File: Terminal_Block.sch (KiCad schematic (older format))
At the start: 0 parts

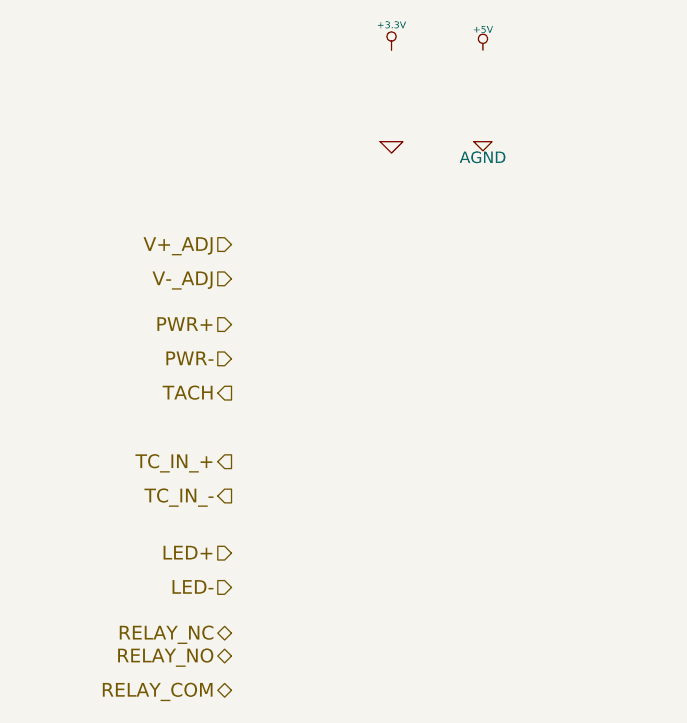
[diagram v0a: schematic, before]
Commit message: Terminal Blocks and ATX Connector
Created footprints for 12pin, 3pin terminal blocks and 24pin ATX Header.
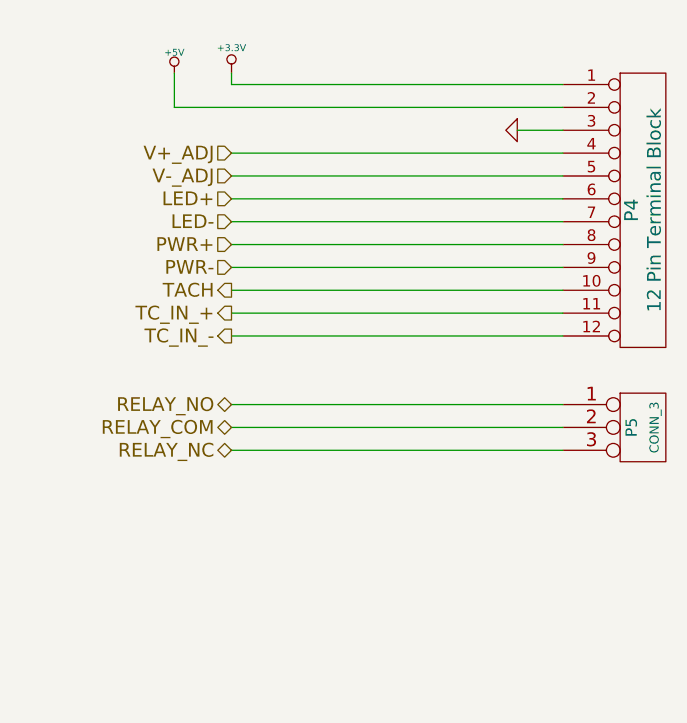
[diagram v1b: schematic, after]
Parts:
- added P4: 12 Pin Terminal Block, symbol CONN_12
- added P5: CONN_3, symbol CONN_3
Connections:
- net +3.3V: now also P4.1 (P1)
- net +5V: now also P4.2 (P2)
- net GND: now also P4.3 (P3)
- net LED+: now also P4.6 (P6)
- net LED-: now also P4.7 (P7)
- net PWR+: now also P4.8 (P8)
- net PWR-: now also P4.9 (P9)
- net RELAY_COM: now also P5.2 (PM)
- net RELAY_NC: now also P5.3 (P3)
- net RELAY_NO: now also P5.1 (P1)
- net TACH: now also P4.10 (P10)
- net TC_IN_+: now also P4.11 (P11)
- net TC_IN_-: now also P4.12 (P12)
- net V+_ADJ: now also P4.4 (P4)
- net V-_ADJ: now also P4.5 (P5)
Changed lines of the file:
@@
 Comment4 ""
 $EndDescr
+Text HLabel 4750 1100 0    60   Input ~ 0
+V+_ADJ
+Text HLabel 4750 1200 0    60   Input ~ 0
+V-_ADJ
 Text HLabel 4750 1500 0    60   Input ~ 0
-V+_ADJ
-Text HLabel 4750 1650 0    60   Input ~ 0
-V-_ADJ
-Text HLabel 4750 1850 0    60   Input ~ 0
 PWR+
-Text HLabel 4750 2000 0    60   Input ~ 0
+Text HLabel 4750 1600 0    60   Input ~ 0
 PWR-
-Text HLabel 4750 2150 0    60   Output ~ 0
+Text HLabel 4750 1700 0    60   Output ~ 0
 TACH
-Text HLabel 4750 2450 0    60   Output ~ 0
-TC_IN_+
-Text HLabel 4750 2600 0    60   Output ~ 0
-TC_IN_-
-Text HLabel 4750 2850 0    60   Input ~ 0
+Text HLabel 4750 1300 0    60   Input ~ 0
 LED+
-Text HLabel 4750 3000 0    60   Input ~ 0
+Text HLabel 4750 1400 0    60   Input ~ 0
 LED-
-Text HLabel 4750 3200 0    60   BiDi ~ 0
+Text HLabel 4750 2400 0    60   BiDi ~ 0
 RELAY_NC
-Text HLabel 4750 3300 0    60   BiDi ~ 0
+Text HLabel 4750 2200 0    60   BiDi ~ 0
 RELAY_NO
-Text HLabel 4750 3450 0    60   BiDi ~ 0
+Text HLabel 4750 2300 0    60   BiDi ~ 0
 RELAY_COM
 $Comp
 L +3.3V #PWR064
 U 1 1 52F91565
-P 5450 650
-F 0 "#PWR064" H 5450 610 30  0001 C CNN
-F 1 "+3.3V" H 5450 760 30  0000 C CNN
-F 2 "" H 5450 650 60  0000 C CNN
-F 3 "" H 5450 650 60  0000 C CNN
-	1    5450 650
+P 4750 750
+F 0 "#PWR064" H 4750 710 30  0001 C CNN
+F 1 "+3.3V" H 4750 860 30  0000 C CNN
+F 2 "" H 4750 750 60  0000 C CNN
+F 3 "" H 4750 750 60  0000 C CNN
+	1    4750 750
 	1    0    0    -1
 $EndComp
@@
 L +5V #PWR065
 U 1 1 52F91574
-P 5850 650
-F 0 "#PWR065" H 5850 740 20  0001 C CNN
-F 1 "+5V" H 5850 740 30  0000 C CNN
-F 2 "" H 5850 650 60  0000 C CNN
-F 3 "" H 5850 650 60  0000 C CNN
-	1    5850 650
+P 4500 750
+F 0 "#PWR065" H 4500 840 20  0001 C CNN
+F 1 "+5V" H 4500 840 30  0000 C CNN
+F 2 "" H 4500 750 60  0000 C CNN
+F 3 "" H 4500 750 60  0000 C CNN
+	1    4500 750
 	1    0    0    -1
 $EndComp
@@
 L GND #PWR066
 U 1 1 52F91583
-P 5450 1050
-F 0 "#PWR066" H 5450 1050 30  0001 C CNN
-F 1 "GND" H 5450 980 30  0001 C CNN
-F 2 "" H 5450 1050 60  0000 C CNN
-F 3 "" H 5450 1050 60  0000 C CNN
-	1    5450 1050
+P 6000 1000
+F 0 "#PWR066" H 6000 1000 30  0001 C CNN
+F 1 "GND" H 6000 930 30  0001 C CNN
+F 2 "" H 6000 1000 60  0000 C CNN
+F 3 "" H 6000 1000 60  0000 C CNN
+	1    6000 1000
+	0    1    1    0
+$EndComp
+$Comp
+L CONN_12 P4
+U 1 1 5309CB10
+P 6550 1350
+F 0 "P4" V 6500 1350 60  0000 C CNN
+F 1 "12 Pin Terminal Block" V 6600 1350 60  0000 C CNN
+F 2 "" H 6550 1350 60  0000 C CNN
+F 3 "" H 6550 1350 60  0000 C CNN
+F 4 "On-Shore Technology" H 6550 1350 60  0001 C CNN "MFG NAME"
+F 5 "OSTTE120104" H 6550 1350 60  0001 C CNN "MFG PART NUM"
+	1    6550 1350
 	1    0    0    -1
 $EndComp
+Wire Wire Line
+	4750 1200 6200 1200
+Wire Wire Line
+	6200 1100 4750 1100
+Wire Wire Line
+	6200 1000 6000 1000
+Wire Wire Line
+	4500 900  6200 900
+Wire Wire Line
+	4500 750  4500 900
+Wire Wire Line
+	4750 800  4750 750
+Wire Wire Line
+	6200 800  4750 800
+Wire Wire Line
+	4750 1300 6200 1300
+Wire Wire Line
+	4750 1400 6200 1400
+Wire Wire Line
+	4750 1500 6200 1500
+Wire Wire Line
+	4750 1600 6200 1600
+Text HLabel 4750 1900 0    60   Output ~ 0
+TC_IN_-
+Text HLabel 4750 1800 0    60   Output ~ 0
+TC_IN_+
+Wire Wire Line
+	4750 1700 6200 1700
+Wire Wire Line
+	4750 1800 6200 1800
+Wire Wire Line
+	4750 1900 6200 1900
 $Comp
-L AGND #PWR067
-U 1 1 52F91592
-P 5850 1050
-F 0 "#PWR067" H 5850 1050 40  0001 C CNN
-F 1 "AGND" H 5850 980 50  0000 C CNN
-F 2 "" H 5850 1050 60  0000 C CNN
-F 3 "" H 5850 1050 60  0000 C CNN
-	1    5850 1050
+L CONN_3 P5
+U 1 1 5309D123
+P 6550 2300
+F 0 "P5" V 6500 2300 50  0000 C CNN
+F 1 "CONN_3" V 6600 2300 40  0000 C CNN
+F 2 "" H 6550 2300 60  0000 C CNN
+F 3 "" H 6550 2300 60  0000 C CNN
+F 4 "PHOENIX CONTACT" H 6550 2300 60  0001 C CNN "MFG NAME"
+F 5 "1935174" H 6550 2300 60  0001 C CNN "MFG PART NUM"
+	1    6550 2300
 	1    0    0    -1
 $EndComp
+Wire Wire Line
+	4750 2200 6200 2200
+Wire Wire Line
+	4750 2300 6200 2300
+Wire Wire Line
+	4750 2400 6200 2400
 $EndSCHEMATC

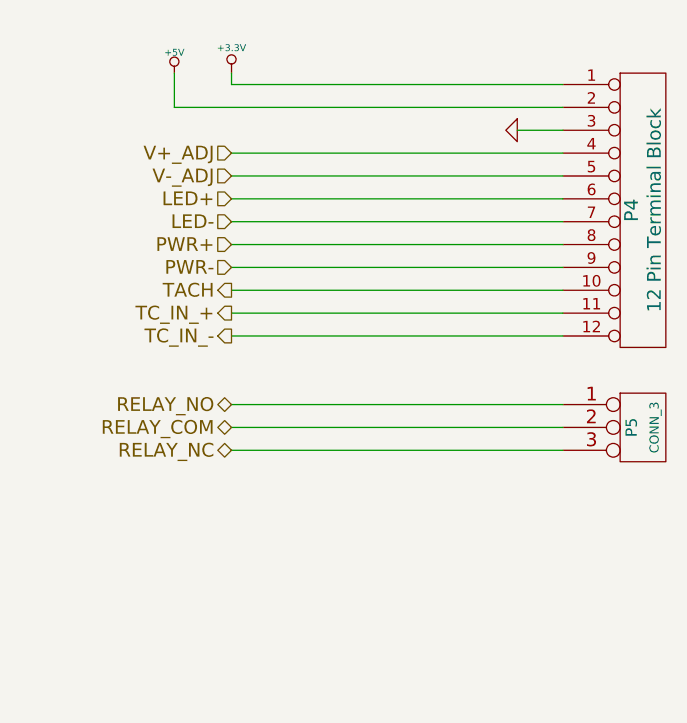
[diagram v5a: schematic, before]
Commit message: Layout v4.0
Adding ground planes according to location of modules
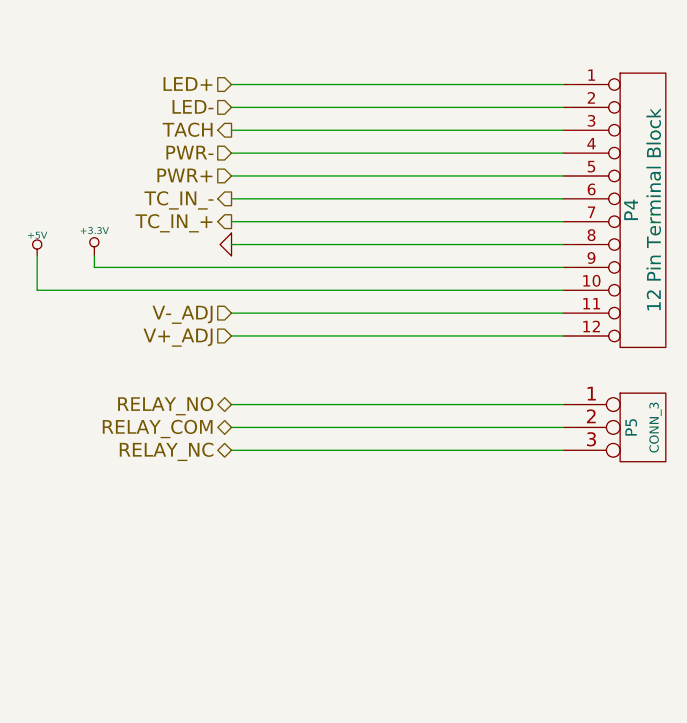
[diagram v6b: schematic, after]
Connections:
- net +3.3V: now also P4.9 (P9); no longer P4.1 (P1)
- net +5V: now also P4.10 (P10); no longer P4.2 (P2)
- net GND: now also P4.8 (P8); no longer P4.3 (P3)
- net LED+: now also P4.1 (P1); no longer P4.6 (P6)
- net LED-: now also P4.2 (P2); no longer P4.7 (P7)
- net PWR+: now also P4.5 (P5); no longer P4.8 (P8)
- net PWR-: now also P4.4 (P4); no longer P4.9 (P9)
- net TACH: now also P4.3 (P3); no longer P4.10 (P10)
- net TC_IN_+: now also P4.7 (P7); no longer P4.11 (P11)
- net TC_IN_-: now also P4.6 (P6); no longer P4.12 (P12)
- net V+_ADJ: now also P4.12 (P12); no longer P4.4 (P4)
- net V-_ADJ: now also P4.11 (P11); no longer P4.5 (P5)
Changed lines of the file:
@@
 Sheet 9 9
 Title ""
-Date "3 mar 2014"
+Date "6 mar 2014"
 Rev ""
 Comp ""
@@
 Comment4 ""
 $EndDescr
+Text HLabel 4750 1900 0    60   Input ~ 0
+V+_ADJ
+Text HLabel 4750 1800 0    60   Input ~ 0
+V-_ADJ
+Text HLabel 4750 1200 0    60   Input ~ 0
+PWR+
 Text HLabel 4750 1100 0    60   Input ~ 0
-V+_ADJ
-Text HLabel 4750 1200 0    60   Input ~ 0
-V-_ADJ
-Text HLabel 4750 1500 0    60   Input ~ 0
-PWR+
-Text HLabel 4750 1600 0    60   Input ~ 0
 PWR-
-Text HLabel 4750 1700 0    60   Output ~ 0
+Text HLabel 4750 1000 0    60   Output ~ 0
 TACH
-Text HLabel 4750 1300 0    60   Input ~ 0
+Text HLabel 4750 800  0    60   Input ~ 0
 LED+
-Text HLabel 4750 1400 0    60   Input ~ 0
+Text HLabel 4750 900  0    60   Input ~ 0
 LED-
 Text HLabel 4750 2400 0    60   BiDi ~ 0
@@
 RELAY_COM
 $Comp
-L +3.3V #PWR062
+L +3.3V #PWR060
 U 1 1 52F91565
-P 4750 750
-F 0 "#PWR062" H 4750 710 30  0001 C CNN
-F 1 "+3.3V" H 4750 860 30  0000 C CNN
-F 2 "" H 4750 750 60  0000 C CNN
-F 3 "" H 4750 750 60  0000 C CNN
-	1    4750 750
+P 4150 1550
+F 0 "#PWR060" H 4150 1510 30  0001 C CNN
+F 1 "+3.3V" H 4150 1660 30  0000 C CNN
+F 2 "" H 4150 1550 60  0000 C CNN
+F 3 "" H 4150 1550 60  0000 C CNN
+	1    4150 1550
 	1    0    0    -1
 $EndComp
 $Comp
-L +5V #PWR063
+L +5V #PWR061
 U 1 1 52F91574
-P 4500 750
-F 0 "#PWR063" H 4500 840 20  0001 C CNN
-F 1 "+5V" H 4500 840 30  0000 C CNN
-F 2 "" H 4500 750 60  0000 C CNN
-F 3 "" H 4500 750 60  0000 C CNN
-	1    4500 750
+P 3900 1550
+F 0 "#PWR061" H 3900 1640 20  0001 C CNN
+F 1 "+5V" H 3900 1640 30  0000 C CNN
+F 2 "" H 3900 1550 60  0000 C CNN
+F 3 "" H 3900 1550 60  0000 C CNN
+	1    3900 1550
 	1    0    0    -1
 $EndComp
 $Comp
-L GND #PWR064
+L GND #PWR062
 U 1 1 52F91583
-P 6000 1000
-F 0 "#PWR064" H 6000 1000 30  0001 C CNN
-F 1 "GND" H 6000 930 30  0001 C CNN
-F 2 "" H 6000 1000 60  0000 C CNN
-F 3 "" H 6000 1000 60  0000 C CNN
-	1    6000 1000
+P 4750 1500
+F 0 "#PWR062" H 4750 1500 30  0001 C CNN
+F 1 "GND" H 4750 1430 30  0001 C CNN
+F 2 "" H 4750 1500 60  0000 C CNN
+F 3 "" H 4750 1500 60  0000 C CNN
+	1    4750 1500
 	0    1    1    0
 $EndComp
@@
 $EndComp
 Wire Wire Line
-	4750 1200 6200 1200
+	3900 1550 3900 1700
 Wire Wire Line
-	6200 1100 4750 1100
-Wire Wire Line
-	6200 1000 6000 1000
-Wire Wire Line
-	4500 900  6200 900
-Wire Wire Line
-	4500 750  4500 900
-Wire Wire Line
-	4750 800  4750 750
-Wire Wire Line
-	6200 800  4750 800
-Wire Wire Line
-	4750 1300 6200 1300
-Wire Wire Line
-	4750 1400 6200 1400
-Wire Wire Line
-	4750 1500 6200 1500
-Wire Wire Line
-	4750 1600 6200 1600
-Text HLabel 4750 1900 0    60   Output ~ 0
+	4150 1600 4150 1550
+Text HLabel 4750 1300 0    60   Output ~ 0
 TC_IN_-
-Text HLabel 4750 1800 0    60   Output ~ 0
+Text HLabel 4750 1400 0    60   Output ~ 0
 TC_IN_+
-Wire Wire Line
-	4750 1700 6200 1700
-Wire Wire Line
-	4750 1800 6200 1800
-Wire Wire Line
-	4750 1900 6200 1900
 $Comp
 L CONN_3 P5
@@
 Wire Wire Line
 	4750 2400 6200 2400
+Wire Wire Line
+	4150 1600 6200 1600
+Wire Wire Line
+	3900 1700 6200 1700
+Wire Wire Line
+	4750 800  6200 800
+Wire Wire Line
+	6200 900  4750 900
+Wire Wire Line
+	4750 1800 6200 1800
+Wire Wire Line
+	4750 1900 6200 1900
+Wire Wire Line
+	4750 1200 6200 1200
+Wire Wire Line
+	6200 1100 4750 1100
+Wire Wire Line
+	4750 1000 6200 1000
+Wire Wire Line
+	6200 1300 4750 1300
+Wire Wire Line
+	4750 1500 6200 1500
+Wire Wire Line
+	4750 1400 6200 1400
 $EndSCHEMATC

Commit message: Layout v5.0
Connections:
- net GND renamed GND_PWR
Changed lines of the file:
@@
 Sheet 9 9
 Title ""
-Date "6 mar 2014"
+Date "8 mar 2014"
 Rev ""
 Comp ""
@@
 	1    3900 1550
 	1    0    0    -1
-$EndComp
-$Comp
-L GND #PWR062
-U 1 1 52F91583
-P 4750 1500
-F 0 "#PWR062" H 4750 1500 30  0001 C CNN
-F 1 "GND" H 4750 1430 30  0001 C CNN
-F 2 "" H 4750 1500 60  0000 C CNN
-F 3 "" H 4750 1500 60  0000 C CNN
-	1    4750 1500
-	0    1    1    0
 $EndComp
 $Comp
@@
 Wire Wire Line
 	4750 1400 6200 1400
+$Comp
+L GND_PWR #PWR062
+U 1 1 53199927
+P 4750 1500
+F 0 "#PWR062" H 4750 1500 30  0001 C CNN
+F 1 "GND_PWR" H 4750 1430 30  0000 C CNN
+F 2 "~" H 4750 1500 60  0000 C CNN
+F 3 "~" H 4750 1500 60  0000 C CNN
+	1    4750 1500
+	0    1    1    0
+$EndComp
 $EndSCHEMATC

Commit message: Layout v6.0
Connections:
- net +3.3V: now also P4.10 (P10); no longer P4.9 (P9)
- net +5V: now also P4.8 (P8); no longer P4.10 (P10)
- net GND_PWR: now also P4.9 (P9); no longer P4.8 (P8)
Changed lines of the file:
@@
 Sheet 9 9
 Title ""
-Date "8 mar 2014"
+Date "9 mar 2014"
 Rev ""
 Comp ""
@@
 RELAY_COM
 $Comp
-L +3.3V #PWR060
+L +3.3V #PWR73
 U 1 1 52F91565
-P 4150 1550
-F 0 "#PWR060" H 4150 1510 30  0001 C CNN
-F 1 "+3.3V" H 4150 1660 30  0000 C CNN
-F 2 "" H 4150 1550 60  0000 C CNN
-F 3 "" H 4150 1550 60  0000 C CNN
-	1    4150 1550
+P 3900 1550
+F 0 "#PWR73" H 3900 1510 30  0001 C CNN
+F 1 "+3.3V" H 3900 1660 30  0000 C CNN
+F 2 "" H 3900 1550 60  0000 C CNN
+F 3 "" H 3900 1550 60  0000 C CNN
+	1    3900 1550
 	1    0    0    -1
 $EndComp
 $Comp
-L +5V #PWR061
+L +5V #PWR74
 U 1 1 52F91574
-P 3900 1550
-F 0 "#PWR061" H 3900 1640 20  0001 C CNN
-F 1 "+5V" H 3900 1640 30  0000 C CNN
-F 2 "" H 3900 1550 60  0000 C CNN
-F 3 "" H 3900 1550 60  0000 C CNN
-	1    3900 1550
+P 4150 1450
+F 0 "#PWR74" H 4150 1540 20  0001 C CNN
+F 1 "+5V" H 4150 1540 30  0000 C CNN
+F 2 "" H 4150 1450 60  0000 C CNN
+F 3 "" H 4150 1450 60  0000 C CNN
+	1    4150 1450
 	1    0    0    -1
 $EndComp
@@
 	3900 1550 3900 1700
 Wire Wire Line
-	4150 1600 4150 1550
+	4150 1500 4150 1450
 Text HLabel 4750 1300 0    60   Output ~ 0
 TC_IN_-
@@
 	4750 2400 6200 2400
 Wire Wire Line
-	4150 1600 6200 1600
+	4150 1500 6200 1500
 Wire Wire Line
 	3900 1700 6200 1700
@@
 	6200 1300 4750 1300
 Wire Wire Line
-	4750 1500 6200 1500
+	4750 1600 6200 1600
 Wire Wire Line
 	4750 1400 6200 1400
 $Comp
-L GND_PWR #PWR062
+L GND_PWR #PWR75
 U 1 1 53199927
-P 4750 1500
-F 0 "#PWR062" H 4750 1500 30  0001 C CNN
-F 1 "GND_PWR" H 4750 1430 30  0000 C CNN
-F 2 "~" H 4750 1500 60  0000 C CNN
-F 3 "~" H 4750 1500 60  0000 C CNN
-	1    4750 1500
+P 4750 1600
+F 0 "#PWR75" H 4750 1600 30  0001 C CNN
+F 1 "GND_PWR" H 4750 1530 30  0000 C CNN
+F 2 "~" H 4750 1600 60  0000 C CNN
+F 3 "~" H 4750 1600 60  0000 C CNN
+	1    4750 1600
 	0    1    1    0
 $EndComp
